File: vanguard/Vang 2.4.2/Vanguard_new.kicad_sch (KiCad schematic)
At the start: 86 parts, among them J1 USB_C_Receptacle_USB2.0_16P, J2 Conn_02x03_Pin, J3 Micro_SD_Card_Det1, J4 STARBOARD_SERVO, J5 PORTSIDE_SERVO, J6 Battery In, J7 EJECTION_SERVO, Q1 BSS138, Q2 BSS138, Q3 BSS138, Q4 BSS138, U1 ATSAMD11D14A-M, U10 BMP390L, U11 BNO055, U2 ATmega4809-A, U3 AT25DF641A-SH-T, U4 AP2112K-3.3, U5 BD1020HFV, U6 TPS82130SILR, U7 TXB0104D, U8 TPS61092, U9 MPM3610AGQV-P, Y2 32.768kHz

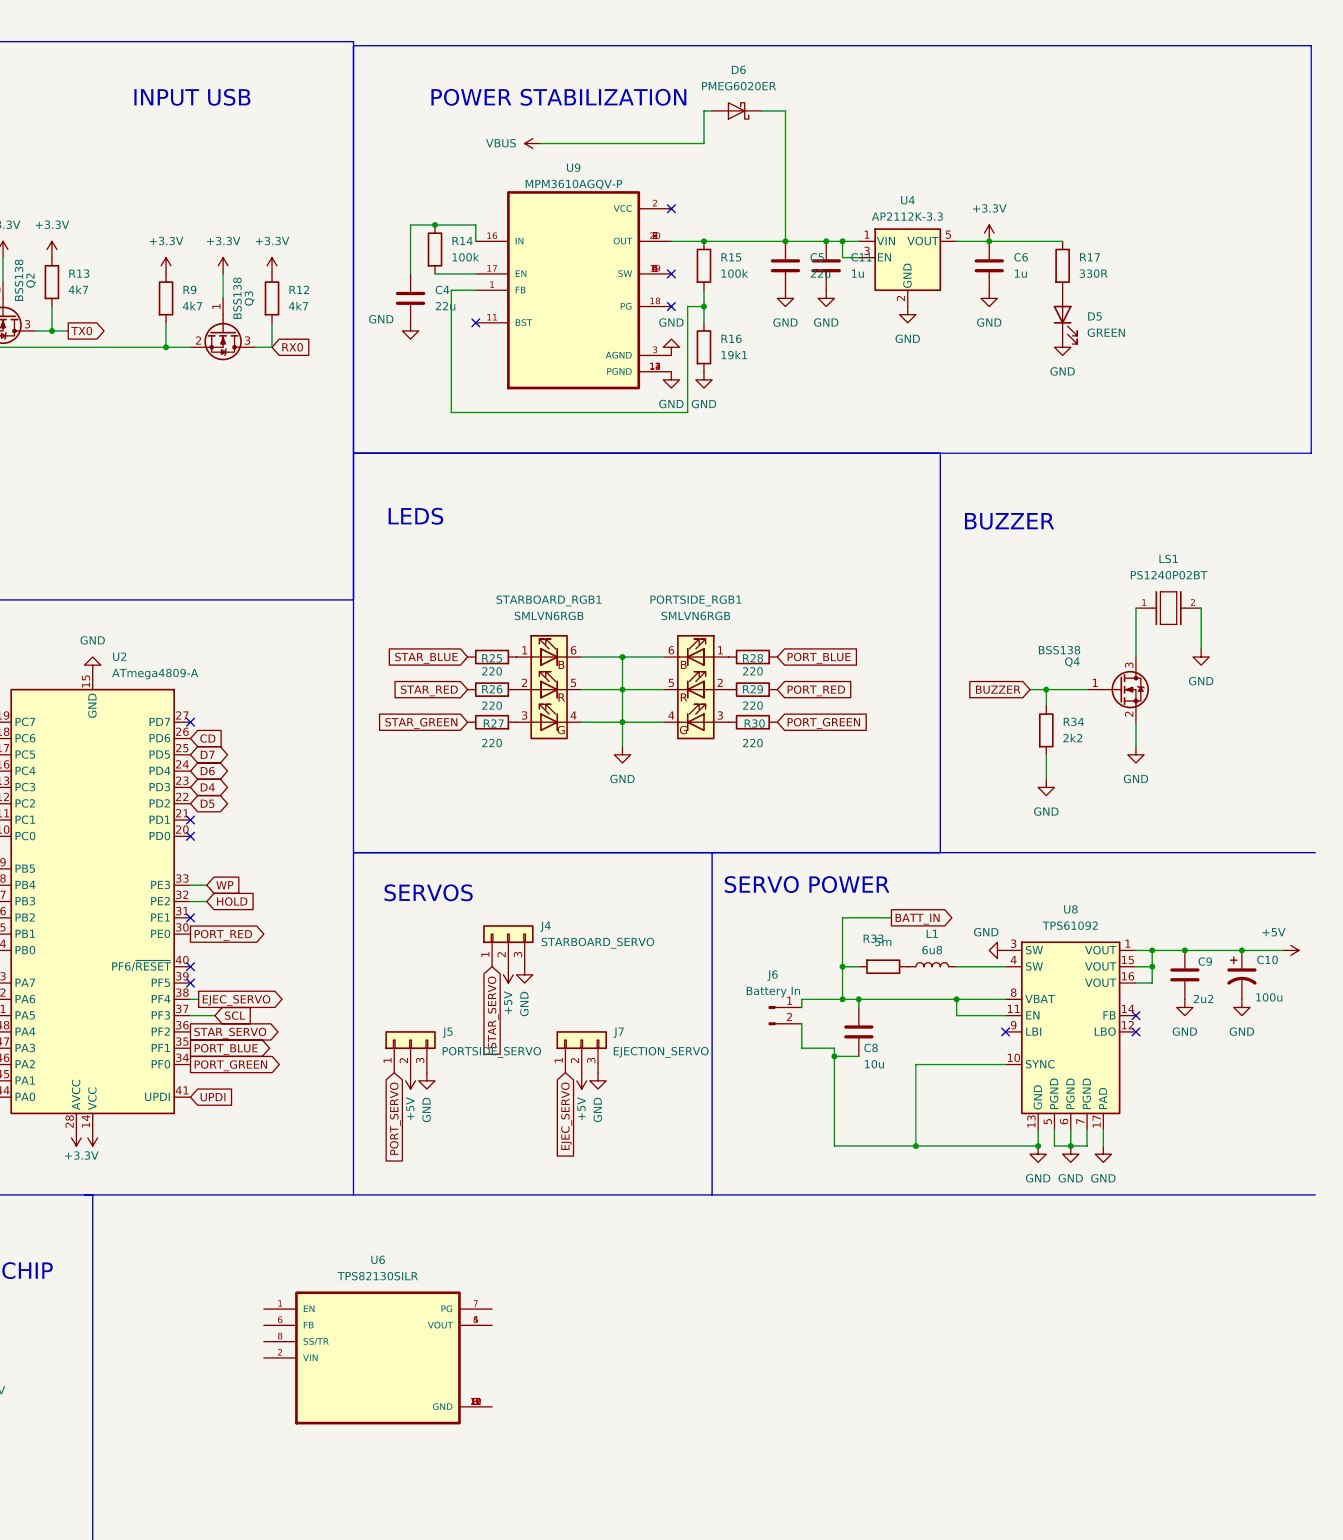
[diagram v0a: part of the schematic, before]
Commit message: Buck convertor schematic done!
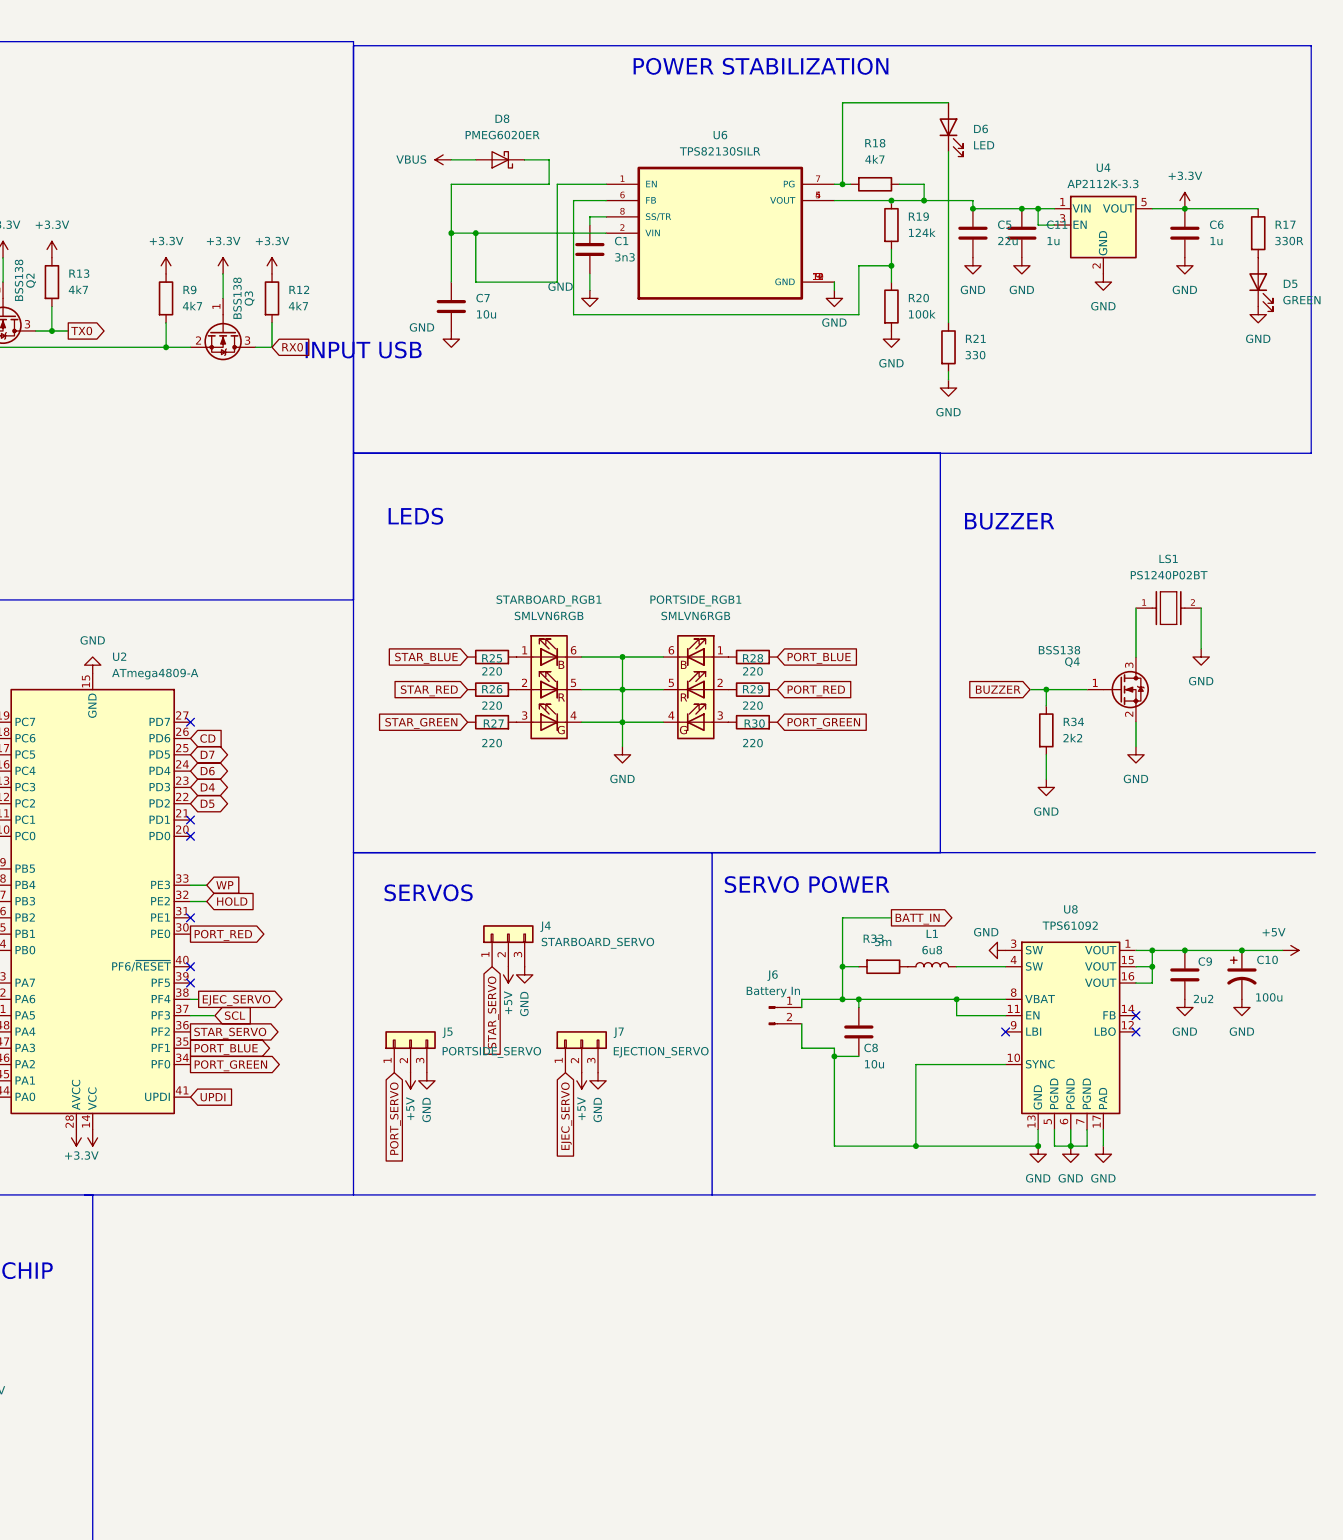
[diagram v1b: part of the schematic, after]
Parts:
- removed C4: 22u, Capacitor_SMD:C_0201_0603Metric, symbol Device:C
- removed D6: PMEG6020ER, Diode_SMD:Nexperia_CFP3_SOD-123W, symbol Diode:PMEG6020ER
- removed R14, R15: 100k, Resistor_SMD:R_0402_1005Metric, symbol Device:R
- removed R16: 19k1, Resistor_SMD:R_0402_1005Metric, symbol Device:R
- removed U9: MPM3610AGQV-P, Package_DFN_QFN:QFN-20-1EP_4x4mm_P0.5mm_EP2.5x2.5mm_ThermalVias, symbol MPM3610AGQV-P:MPM3610AGQV-P
- added C1: 3n3, symbol Device:C
- added C7: 10u, Capacitor_SMD:C_0201_0603Metric, symbol Device:C
- added D6: LED, symbol Device:LED
- added D8: PMEG6020ER, Diode_SMD:Nexperia_CFP3_SOD-123W, symbol Diode:PMEG6020ER
- added R18: 4k7, Resistor_SMD:R_0402_1005Metric, symbol Device:R
- added R19: 124k, Resistor_SMD:R_0402_1005Metric, symbol Device:R
- added R20: 100k, Resistor_SMD:R_0402_1005Metric, symbol Device:R
- added R21: 330, Resistor_SMD:R_0402_1005Metric, symbol Device:R
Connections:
- net GND: now also U6.10 (GND), U6.11 (GND), U6.12 (GND), U6.3 (GND), U6.9 (GND), C1.2, C7.2, R20.2, R21.2
- net VBUS: now also D8.2 (A)
- net at C11.1, C5.1, U4.1 (VIN)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: now also U6.4 (VOUT), U6.5 (VOUT), R18.1, R19.1
- net at U6.1 (EN): now also U6.2 (VIN), C7.1, D8.1 (K)
- net at U6.6 (FB): now also R19.2, R20.1
- net at U6.7 (PG): now also D6.2 (A), R18.2
- net at U6.8 (SS/TR): now also C1.1
- new net: D6.1 (K), R21.1
- no-connect marks 46 -> 42
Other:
- moved on the sheet: C11, C5, C6, D5, R17, U4, U6

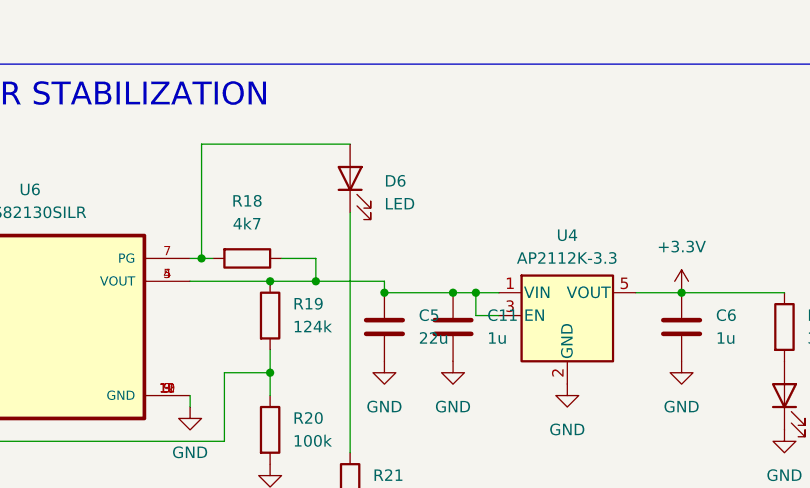
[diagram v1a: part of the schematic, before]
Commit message: added an led footprint
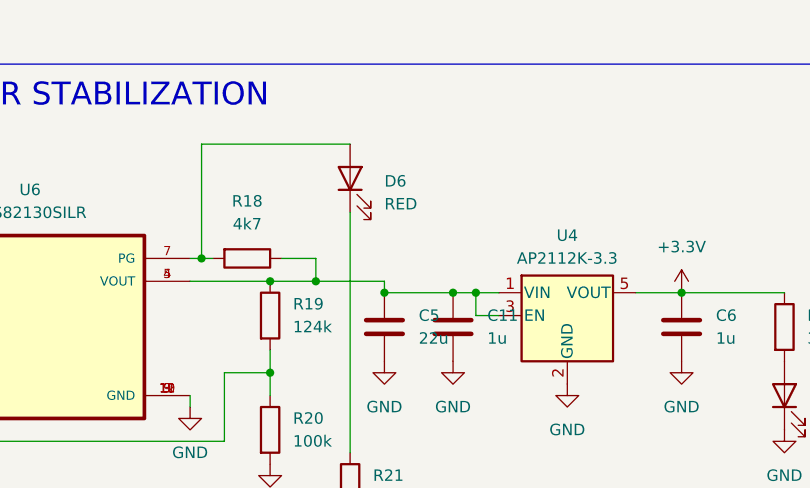
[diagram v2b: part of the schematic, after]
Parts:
- D6: value LED -> RED; footprint (none) -> LED_SMD:LED_0201_0603Metric
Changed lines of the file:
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@@
 			)
 		)
-		(property "Value" "LED"
+		(property "Value" "RED"
 			(at 365.76 29.5274 90)
 			(effects
@@
 			)
 		)
-		(property "Footprint" ""
+		(property "Footprint" "LED_SMD:LED_0201_0603Metric"
 			(at 361.95 26.67 0)
 			(effects

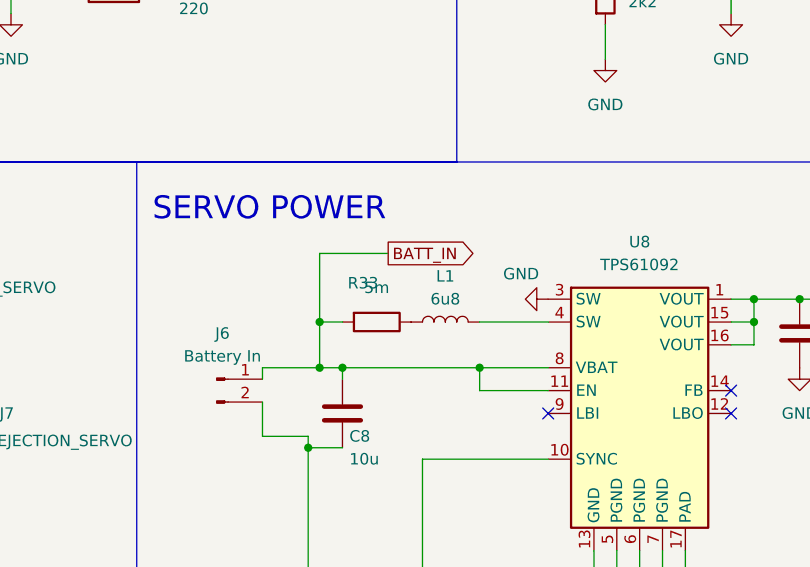
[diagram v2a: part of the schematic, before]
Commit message: Changed resistor
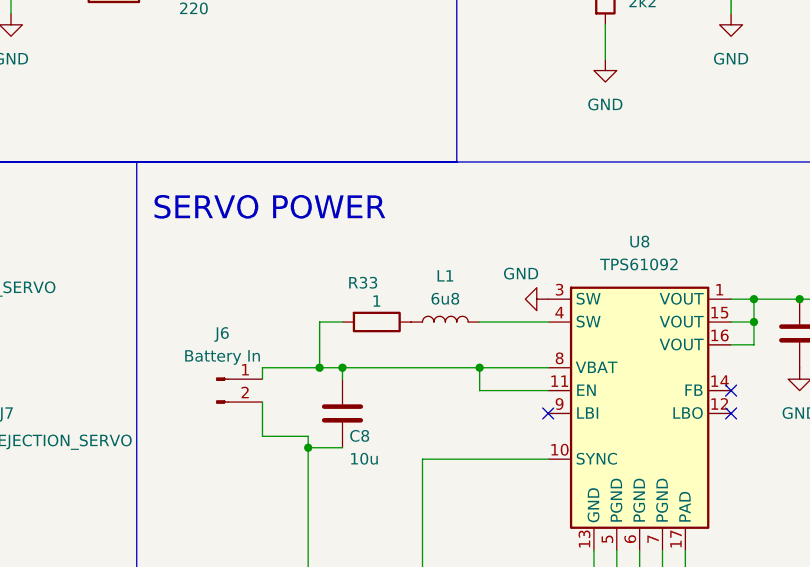
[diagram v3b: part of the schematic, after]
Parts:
- R33: value 5m -> 1
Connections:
- net VBUS: no longer C8.1, J6.1 (Pin_1), R33.2, U8.11 (EN), U8.8 (VBAT)
- new net: C8.1, J6.1 (Pin_1), R33.2, U8.11 (EN), U8.8 (VBAT)
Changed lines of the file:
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@@
 	)
 	(junction
-		(at 345.44 157.48)
-		(diameter 0)
-		(color 0 0 0 0)
-	)
-	(junction
 		(at 71.12 36.83)
 		(diameter 0)
@@
 	(wire
 		(pts
-			(xy 345.44 149.86) (xy 345.44 157.48)
-		)
-		(stroke
-			(width 0)
-			(type default)
-		)
-	)
-	(wire
-		(pts
 			(xy 93.98 160.02) (xy 109.22 160.02)
 		)
@@
 	(wire
 		(pts
-			(xy 353.06 149.86) (xy 345.44 149.86)
-		)
-		(stroke
-			(width 0)
-			(type default)
-		)
-	)
-	(wire
-		(pts
 			(xy 59.69 234.95) (xy 59.69 233.68)
 		)
@@
 		)
 	)
-	(global_label "BATT_IN"
-		(shape output)
-		(at 353.06 149.86 0)
-		(fields_autoplaced yes)
-		(effects
-			(font
-				(size 1.27 1.27)
-			)
-			(justify left)
-		)
-		(property "Intersheetrefs" "${INTERSHEET_REFS}"
-			(at 363.2419 149.86 0)
-			(effects
-				(font
-					(size 1.27 1.27)
-				)
-				(justify left)
-				(hide yes)
-			)
-		)
-	)
 	(global_label "PA1{slash}MOSI"
 		(shape input)
@@
 			)
 		)
-		(property "Value" "5m"
-			(at 351.79 153.67 90)
+		(property "Value" "1"
+			(at 351.79 155.194 90)
 			(effects
 				(font

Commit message: Assigned some footprints and annotated
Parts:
- removed LS1: PS1240P02BT, PS1240P02BT:XDCR_PS1240P02BT, symbol PS1240P02BT[1]:PS1240P02BT
- added LS1: CMI-1295-0585T, CMI-1295-0585T:CUI_CMI-1295-0585T, symbol CMI-1295-0585T[1]:CMI-1295-0585T
- C1: renamed from C12; value 4n7 -> C
- C10: renamed from C11; value 1u -> C
- C11: renamed from C6; value 1u -> C
- C12: renamed from C9; value 2u2 -> C
- C13: renamed from C10; value 100u -> C_Polarized_US
- C2: renamed from C13; value 100n -> C
- C3: renamed from C16; value 0u1 -> C
- C4: renamed from C14; value 22p -> C
- C5: renamed from C15; value 22p -> C
- C6: renamed from C7; value 10u -> C
- C7: renamed from C1; value 3n3 -> C; footprint (none) -> Capacitor_SMD:C_0201_0603Metric
- C8: value 10u -> C
- C9: renamed from C5; value 22u -> C
- D10: renamed from D5; value GREEN -> LED
- D4: value DNP -> D_Zener
- D9: renamed from D6; value RED -> LED
- J3: renamed from J2; value Conn_02x03_Pin -> Conn_02x03_Odd_Even
- J4: renamed from J5; value PORTSIDE_SERVO -> Conn_01x03
- J5: renamed from J4; value STARBOARD_SERVO -> Conn_01x03
- J6: renamed from J7; value EJECTION_SERVO -> Conn_01x03
- J7: renamed from J6; value Battery In -> Conn_01x02_Pin
- L1: value 6u8 -> L
- R1: renamed from R38; value 2k2 -> R
- R10: renamed from R1; value 4.7kΩ -> R
- R11: renamed from R4; value 330 -> R
- R12: renamed from R5; value 0 -> R
- R13: renamed from R3; value 330 -> R
- R14: renamed from R6; value 4k7 -> R
- R15: renamed from R8; value DNP -> R
- R16: renamed from R7; value 4k7 -> R
- R17: renamed from R10; value 4k7 -> R
- R18: renamed from R13; value 4k7 -> R
- R19: renamed from R9; value 4k7 -> R
- R2: renamed from R39; value 2k2 -> R
- R20: renamed from R12; value 4k7 -> R
- R21: renamed from R25; value 220 -> R
- R22: renamed from R26; value 220 -> R
- R23: renamed from R27; value 220 -> R
- R24: renamed from R28; value 220 -> R
- R25: renamed from R29; value 220 -> R
- R26: renamed from R30; value 220 -> R
- R27: renamed from R18; value 4k7 -> R
- R28: renamed from R33; value 1 -> R
- R29: renamed from R19; value 124k -> R
- R3: renamed from R37; value 10k -> R
- R30: renamed from R20; value 100k -> R
- R31: renamed from R21; value 330 -> R
- R32: renamed from R34; value 2k2 -> R
- R33: renamed from R17; value 330R -> R
- R4: renamed from R35; value R220 -> R
- R5: renamed from R31; value 5k1 -> R
- R6: renamed from R32; value 5k1 -> R
- R7: renamed from R36; value 4.7kΩ -> R
- R8: renamed from R11; value 4k7 -> R
- R9: renamed from R2; value 4k7 -> R
- U9: renamed from U8; footprint Package_DFN_QFN:DFN-10-1EP_3x3mm_P0.5mm_EP1.65x2.38mm_ThermalVias -> Package_DFN_QFN:Texas_RSA_VQFN-16-1EP_4x4mm_P0.65mm_EP2.7x2.7mm_ThermalVias
- Y1: renamed from Y2; value 32.768kHz -> Crystal
- renumbered D7 to D1, D1 to D2, D2 to D3, D3 to D5, D8 to D6, STARBOARD_RGB1 to D7, PORTSIDE_RGB1 to D8, J3 to J2, JP2 to JP1, JP1 to JP2, TP3 to TP1, TP9 to TP2, TP1 to TP3, TP2 to TP4, TP8 to TP5, TP4 to TP6, U7 to U1, U4 to U10, U11 to U2, U1 to U3, U10 to U4, U3 to U6, U2 to U7, U6 to U8
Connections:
- net GND: now also LS1.N
- net at Q4.3 (D): now also LS1.P

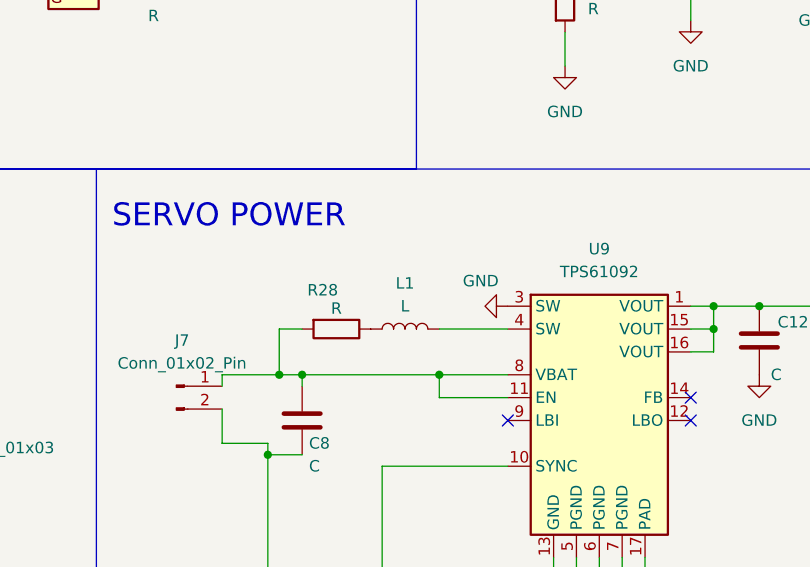
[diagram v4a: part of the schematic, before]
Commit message: Added inductor attributes
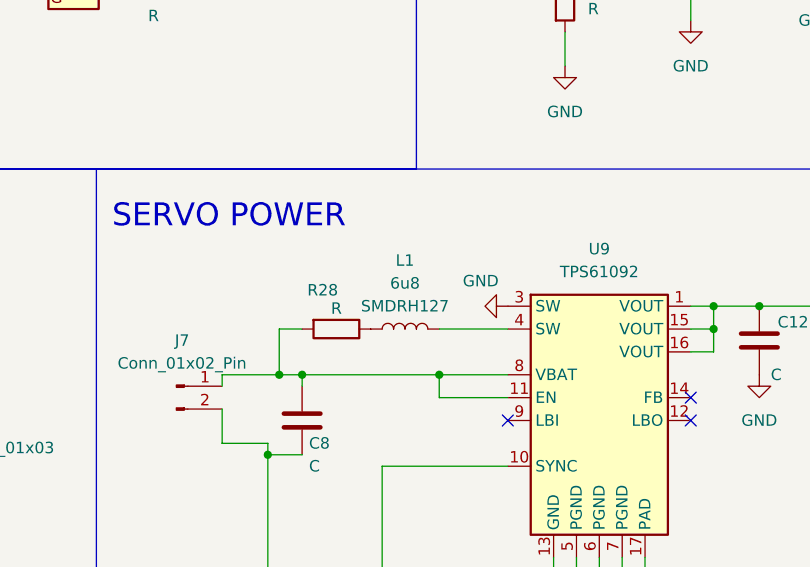
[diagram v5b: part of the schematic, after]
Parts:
- L1: value L -> 6u8
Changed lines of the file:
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@@
 		(fields_autoplaced yes)
 		(property "Reference" "L1"
-			(at 359.41 152.4 90)
+			(at 359.41 149.86 90)
 			(effects
 				(font
@@
 			)
 		)
-		(property "Value" "L"
-			(at 359.41 154.94 90)
+		(property "Value" "6u8"
+			(at 359.41 152.4 90)
 			(effects
 				(font
@@
 			)
 		)
-		(property "Description" "Inductor"
-			(at 359.41 157.48 0)
+		(property "Description" "SMDRH127"
+			(at 359.41 154.94 90)
 			(effects
 				(font
 					(size 1.27 1.27)
 				)
-				(hide yes)
 			)
 		)
